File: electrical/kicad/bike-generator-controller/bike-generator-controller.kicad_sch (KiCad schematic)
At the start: 0 parts

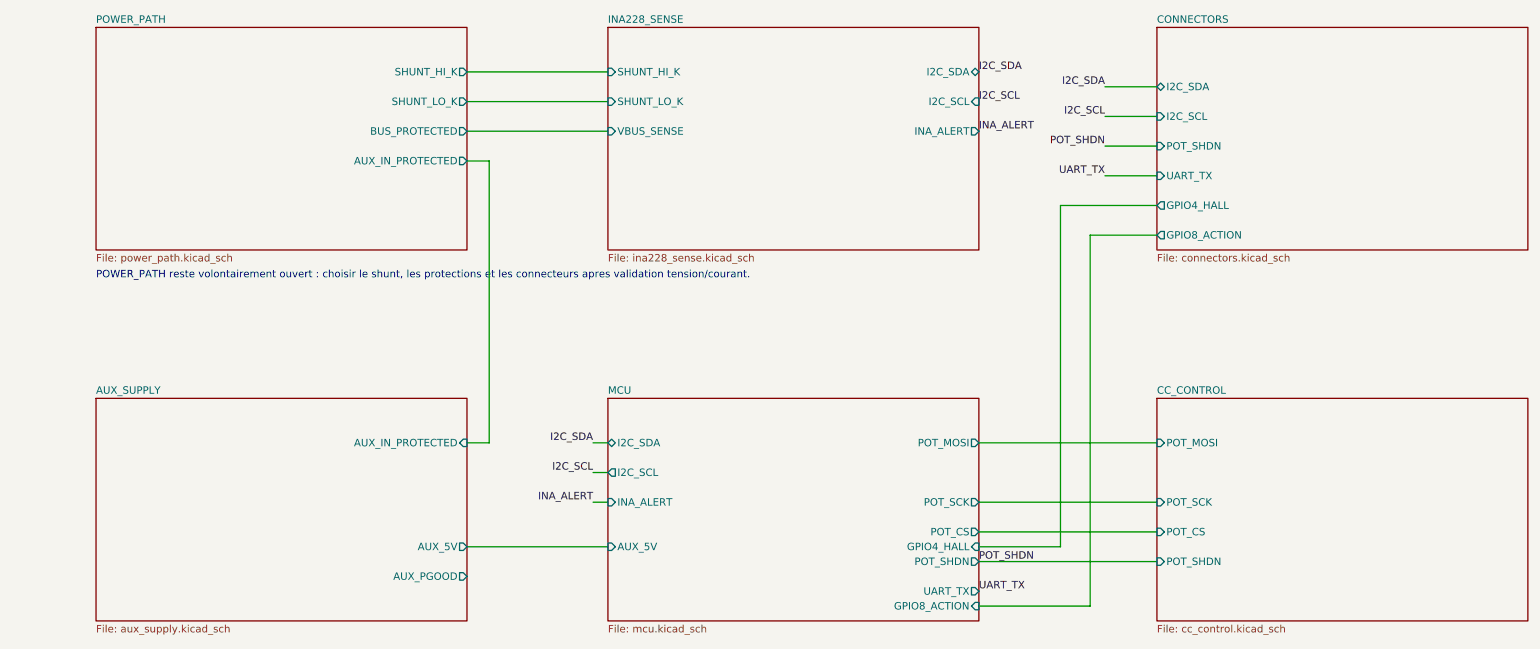
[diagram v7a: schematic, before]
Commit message: feat: close controller v1 design and define integrated v2
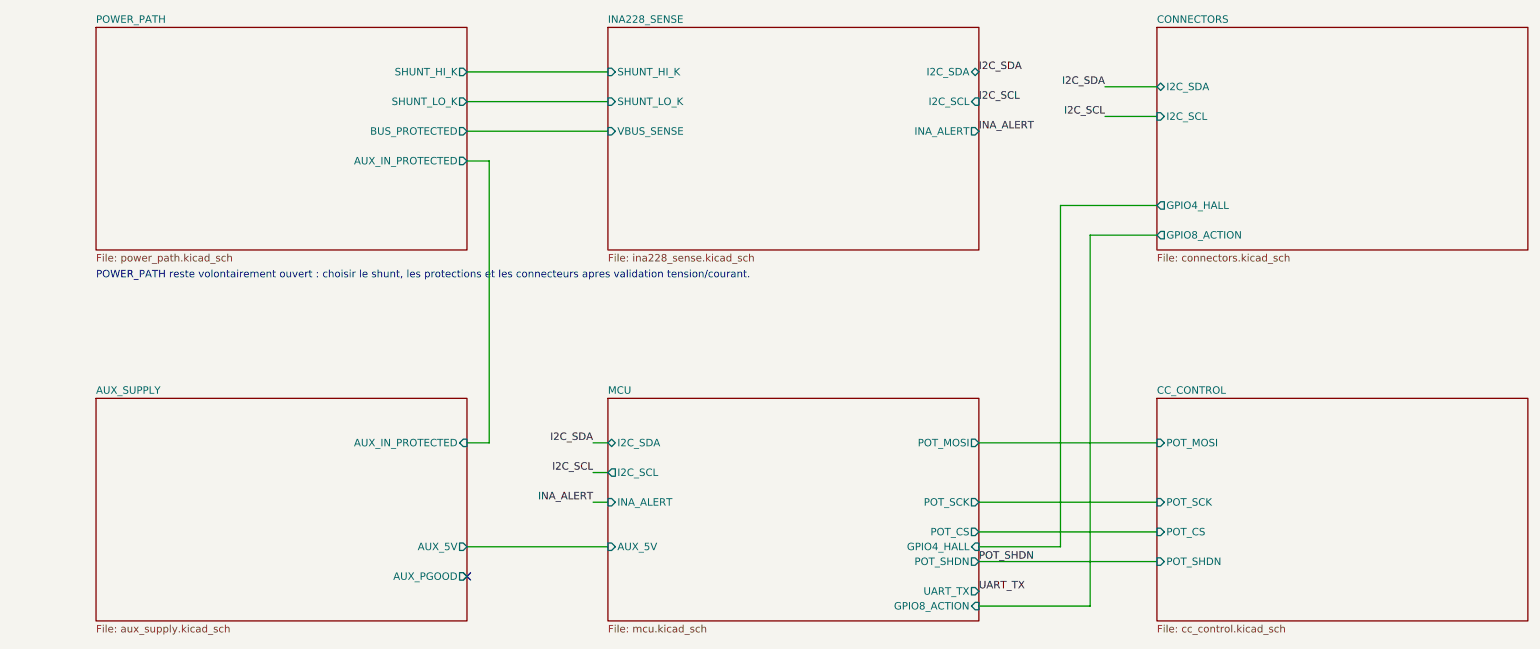
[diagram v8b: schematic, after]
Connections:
- no-connect marks 0 -> 1
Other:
- sheet CONNECTORS ports: added none; removed POT_SHDN, UART_TX
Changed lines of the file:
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@@
 		)
+	)
+	(no_connect
+		(at 88.9 132.08)
 	)
 	(wire
@@
 	(wire
 		(pts
-			(xy 207.01 58.42) (xy 198.12 58.42)
-		)
-		(stroke
-			(width 0)
-			(type default)
-		)
-	)
-	(wire
-		(pts
 			(xy 113.03 119.38) (xy 110.49 119.38)
 		)
@@
 		(pts
 			(xy 176.53 124.46) (xy 207.01 124.46)
-		)
-		(stroke
-			(width 0)
-			(type default)
-		)
-	)
-	(wire
-		(pts
-			(xy 207.01 63.5) (xy 198.12 63.5)
 		)
 		(stroke
@@
 		)
 	)
-	(label "UART_TX"
-		(at 198.12 63.5 180)
-		(effects
-			(font
-				(size 1.27 1.27)
-			)
-			(justify right bottom)
-		)
-	)
 	(label "I2C_SCL"
 		(at 198.12 53.34 180)
@@
 			)
 			(justify left bottom)
-		)
-	)
-	(label "POT_SHDN"
-		(at 198.12 58.42 180)
-		(effects
-			(font
-				(size 1.27 1.27)
-			)
-			(justify right bottom)
 		)
 	)
@@
 			(effects
 				(font
-					(size 1.27 1.27)
-				)
-				(justify left)
-			)
-		)
-		(pin "UART_TX" input
-			(at 207.01 63.5 180)
-			(effects
-				(font
-					(size 1.27 1.27)
-				)
-				(justify left)
-			)
-		)
-		(pin "POT_SHDN" input
-			(at 207.01 58.42 180)
-			(effects
-				(font
